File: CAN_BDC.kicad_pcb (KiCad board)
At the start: 2 copper layers, 24.5 x 34 mm, 28 parts, among them P1 CONN_01X02, P2 CONN_01X05, P4 CONN_01X04, P5 CONN_01X04, P6 CONN_01X02, P7 CONN_01X04, P8 CONN_01X04, P9 CONN_01X02, U1 PSD2CAN, U2 SN65HVD232D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

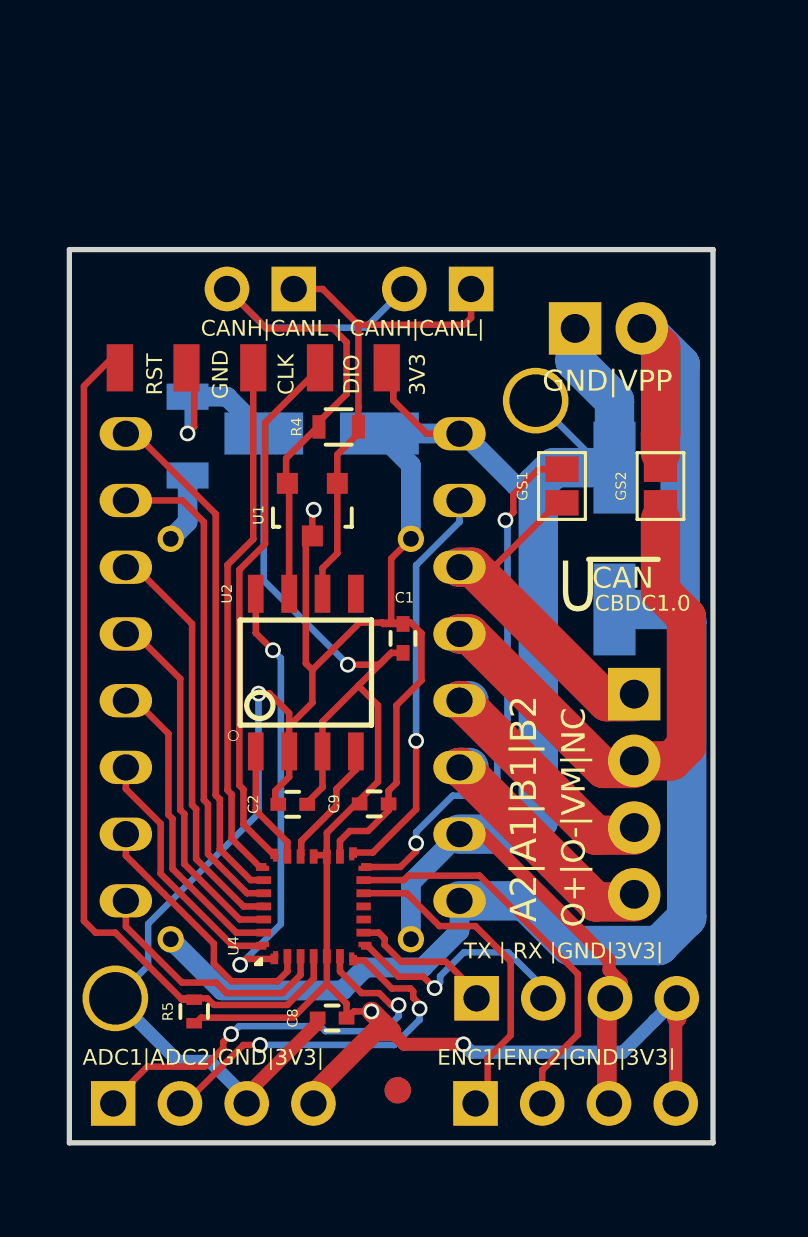
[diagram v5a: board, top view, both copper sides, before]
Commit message: regulator addition
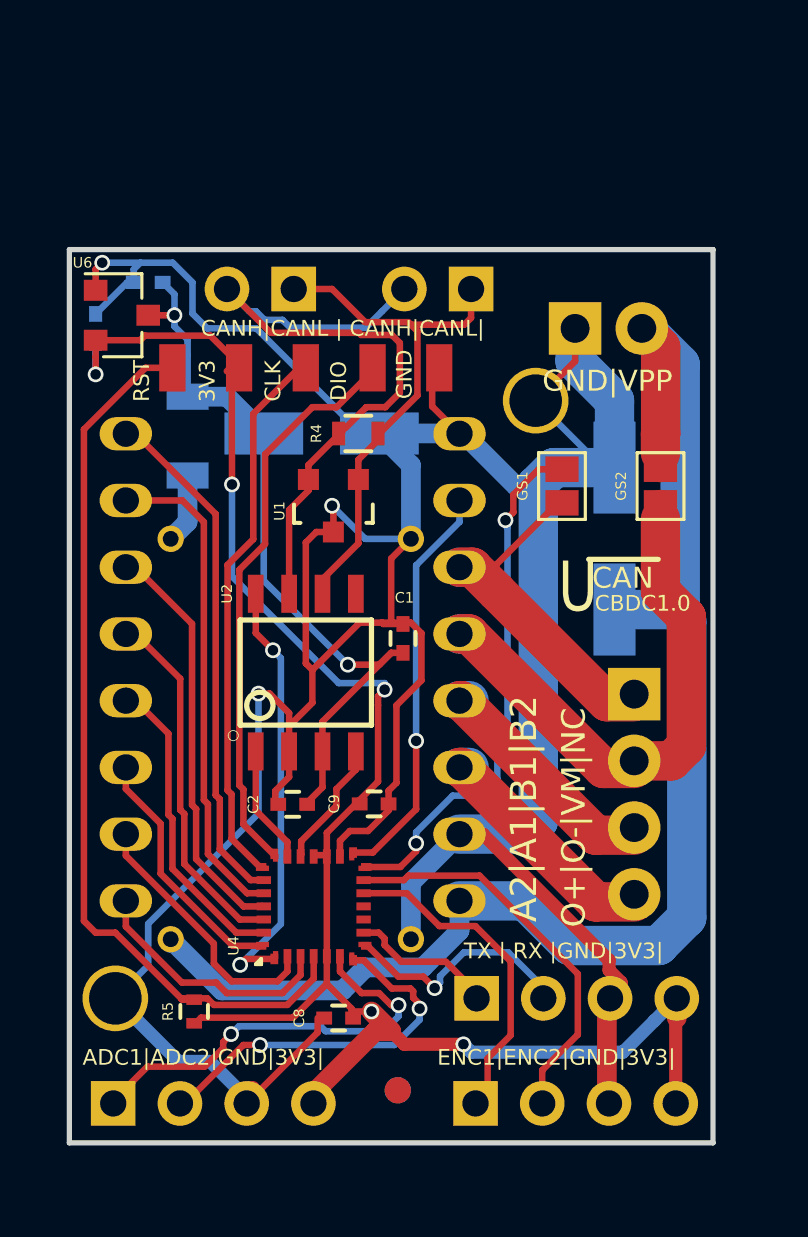
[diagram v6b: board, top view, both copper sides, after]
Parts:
- added C3: 1u, Capacitors_SMD:C_0402, B.Cu at (141.7, 79.5)
- added C5: 1u, Capacitors_SMD:C_0402, B.Cu at (139.7, 81.3)
- added U6: MCP1700T-3302E/TT, TO_SOT_Packages_SMD:SOT-23, F.Cu at (140.7, 80.8)
- moved P2 2.00 mm to (149.0, 82.8)
- moved U1 0.81 mm to (148.8, 88.1)
- moved R4 0.79 mm to (149.7, 85.3)
- moved C8 0.25 mm to (148.9, 107.5)
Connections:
- C1 pad 1: +3V3 -> +5V
- C2 pad 1: +3V3 -> +5V
- C7 pad 1: +3V3 -> +5V
- L2 pad 2: +3V3 -> +5V
- U2 pad 3: +3V3 -> +5V
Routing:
- net +5V: track 0.00 -> 29.1 mm, vias 0 -> 2
- net GND: track 123.3 -> 148.4 mm, vias 2 -> 3
- net +3V3: track 71.0 -> 67.3 mm, vias 4 -> 5
- net Net-(P1-Pad2): track 24.4 -> 27.2 mm
- net SW_DIO: track 20.4 -> 21.7 mm
- net Net-(P1-Pad1): track 19.8 -> 20.6 mm
- net SW_CLK: track 21.3 -> 20.8 mm

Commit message: Capacitor placment update
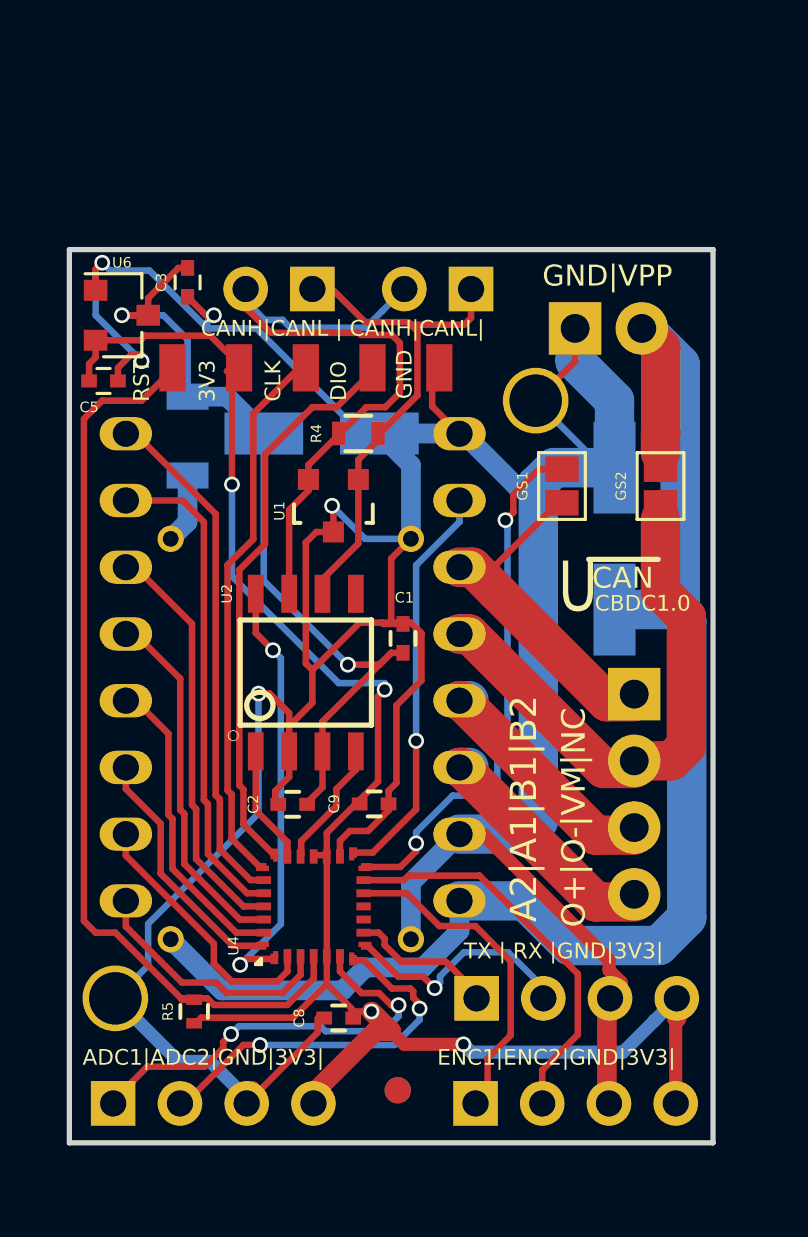
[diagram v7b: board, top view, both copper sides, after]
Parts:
- C3, C5: moved to F.Cu
- moved C5 2.02 mm to (140.0, 83.3), turned to 0 degrees
- moved C3 1.50 mm to (143.2, 79.5), turned to 270 degrees
- moved P1 0.71 mm to (147.9, 79.8)
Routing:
- net GND: track 148.4 -> 153.2 mm, vias 3 -> 5
- net +5V: track 29.1 -> 32.1 mm
- net +3V3: track 67.3 -> 66.5 mm, vias 5 -> 4

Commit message: Gerber Files generation
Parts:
- P2: footprint usb_ccb_custom:swd_smd_conn5 -> Pin_Headers:Pin_Header_Straight_1x05_Pitch1.27mm_SMD_Pin1Left
- moved P2 4.28 mm to (145.3, 85.0), turned to 270 degrees
- moved R4 0.35 mm to (150.1, 85.3)
- moved U1 0.20 mm to (148.9, 88.1)
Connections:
- P2 pad 3: SW_CLK -> +3V3
- P2 pad 4: +3V3 -> SW_CLK
- U2 pad 5: (no net) -> Net-(U2-Pad5)
- U4 pad 10: (no net) -> Net-(U4-Pad10)
- U4 pad 11: (no net) -> Net-(U4-Pad11)
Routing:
- net Net-(P1-Pad2): track 27.2 -> 19.4 mm, vias 0 -> 1
- net SW_DIO: track 21.7 -> 15.6 mm
- net SW_CLK: track 20.8 -> 15.7 mm
- net Net-(P1-Pad1): track 20.6 -> 22.1 mm
- net GND: track 153.2 -> 152.8 mm, vias 5 -> 6
